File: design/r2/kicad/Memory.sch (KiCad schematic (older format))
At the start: 8 parts, among them U1 SST39SF040, U2 SST39SF040, U3 AS6C4008-55PCN, U4 AS6C4008-55PCN

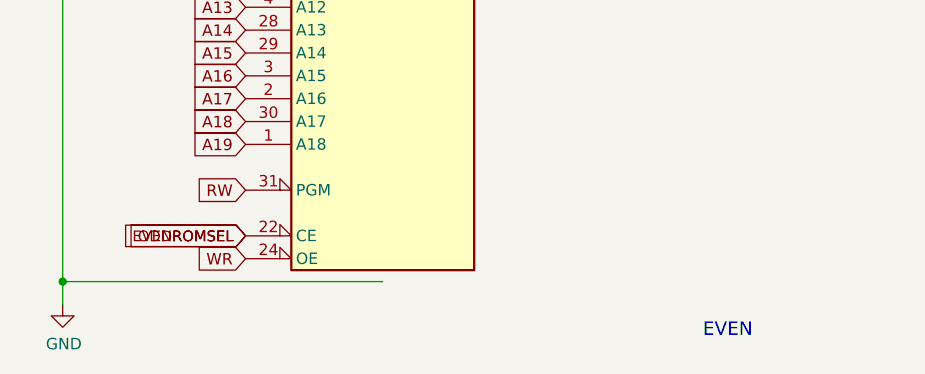
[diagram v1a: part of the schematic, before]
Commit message: Schematic / GAL tweaks and do layout
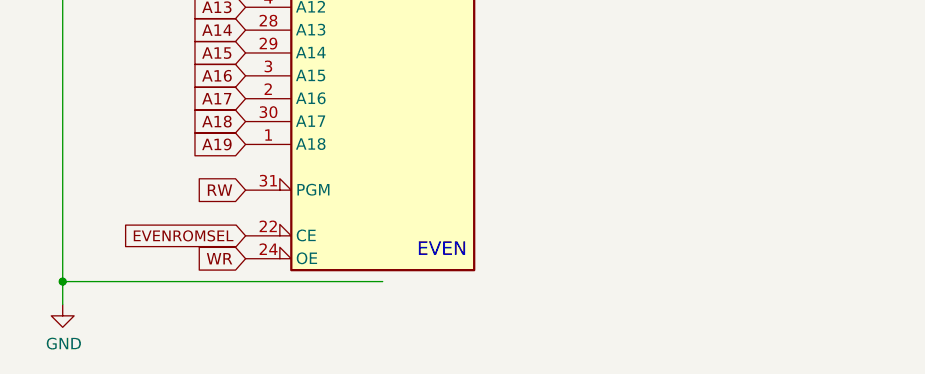
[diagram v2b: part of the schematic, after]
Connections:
- net EVENROMSEL: no longer U1.22 (CE)
- new net ODDROMSEL: U1.22 (CE)
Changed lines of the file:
@@
 Text Notes 6200 3900 0    59   ~ 0
 ODD
-Text Notes 3800 7600 0    59   ~ 0
+Text Notes 2550 7250 0    59   ~ 0
 EVEN
 Text Notes 9600 3900 0    59   ~ 0
@@
 Text GLabel 1800 7250 0    50   Input ~ 0
 WR
-Text GLabel 1800 7150 0    47   Input ~ 0
-ODDROMSEL
 $Comp
 L power:VCC #PWR0105

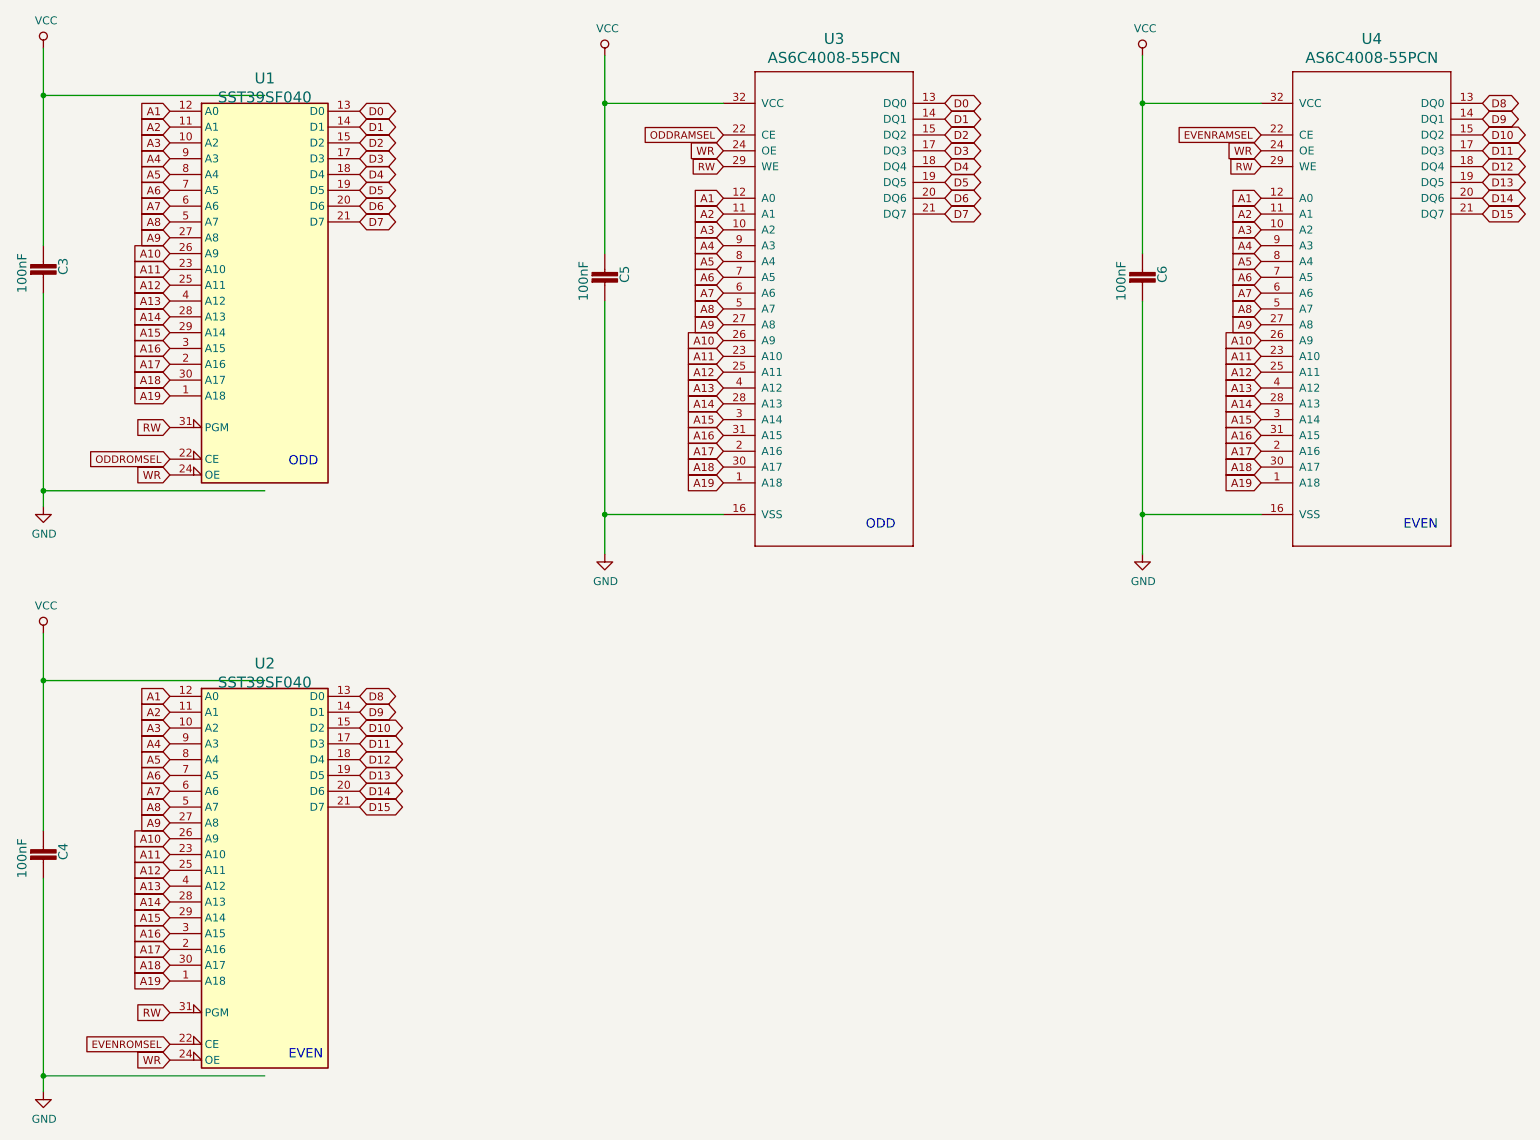
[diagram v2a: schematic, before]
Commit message: Add ROM write-enable jumper and tidy up
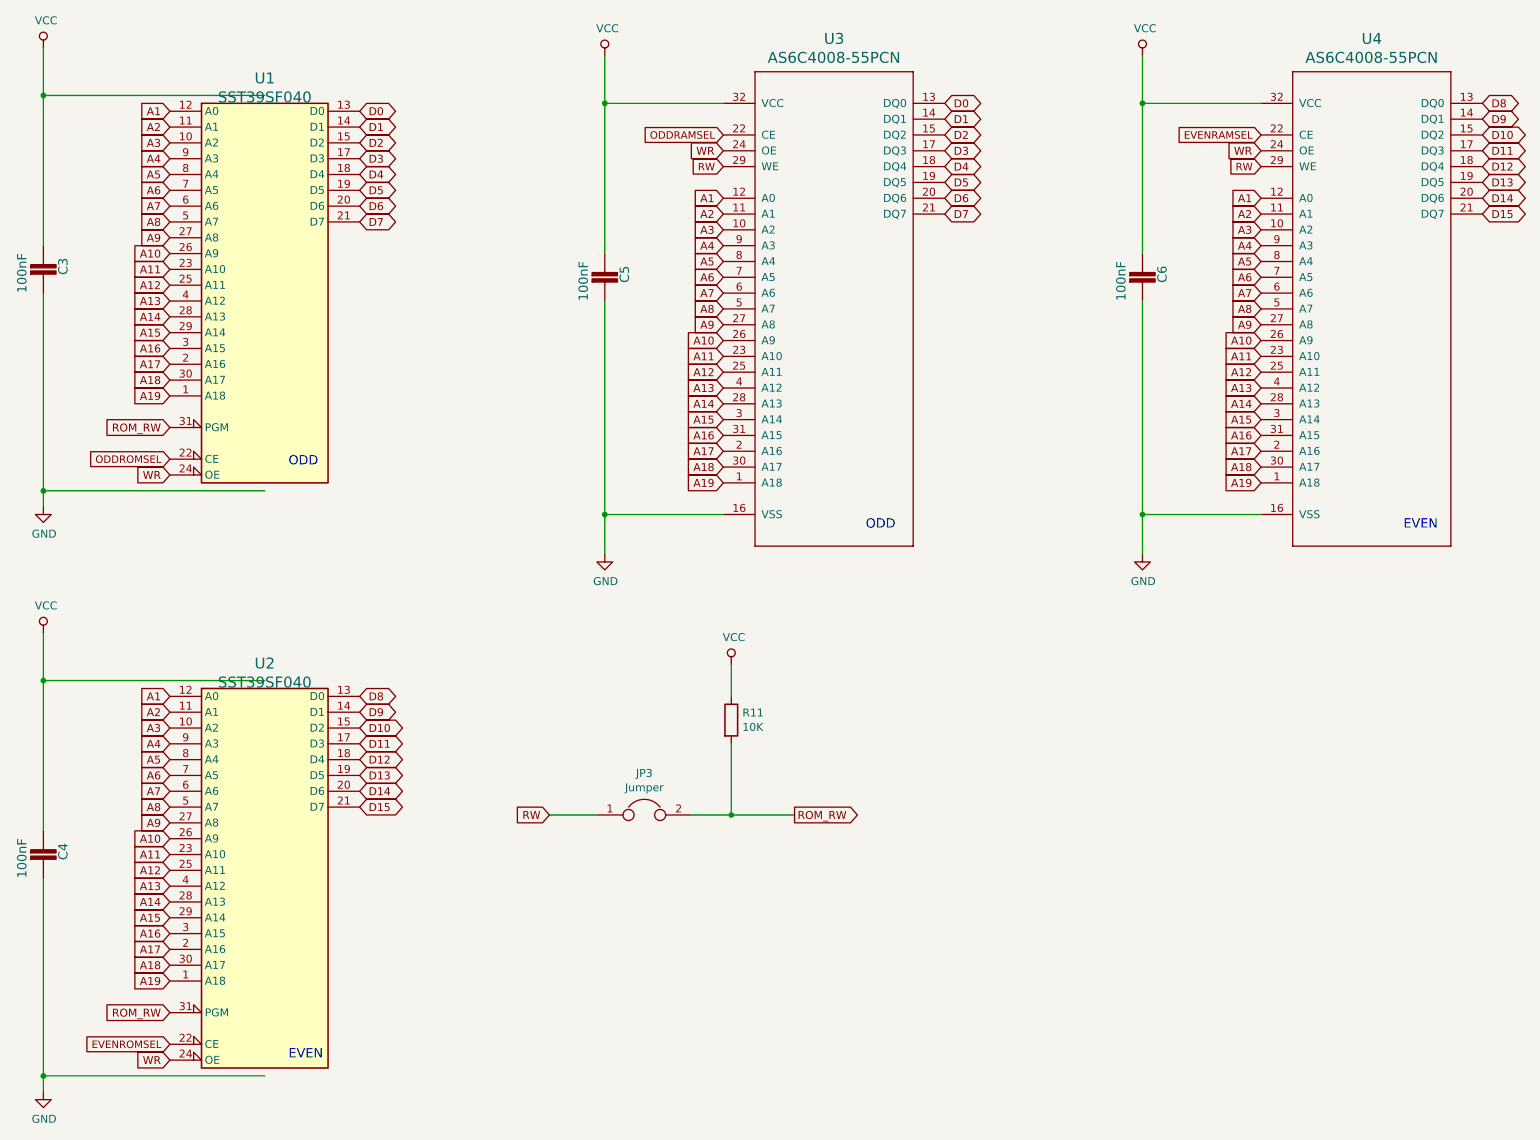
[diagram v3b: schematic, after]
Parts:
- added JP3: Jumper, rosco_m68k:1X02, symbol Device:Jumper
- added R11: 10K, rosco_m68k:0207_10, symbol Device:R
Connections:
- net RW: now also JP3.1; no longer U1.31 (PGM), U2.31 (PGM)
- net VCC: now also R11.1
- new net ROM_RW: JP3.2, R11.2, U1.31 (PGM), U2.31 (PGM)
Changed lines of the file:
@@
 D7
 Text GLabel 1800 3250 0    50   Input ~ 0
-RW
+ROM_RW
 Text GLabel 1800 3550 0    50   Input ~ 0
 WR
@@
 A19
 Text GLabel 1800 6950 0    50   Input ~ 0
-RW
+ROM_RW
 Text GLabel 1800 7250 0    50   Input ~ 0
 WR
@@
 Text GLabel 5300 1500 0    50   Input ~ 0
 WR
+$Comp
+L Device:Jumper JP3
+U 1 1 6162CC16
+P 4800 5700
+F 0 "JP3" H 4800 5964 50  0000 C CNN
+F 1 "Jumper" H 4800 5873 50  0000 C CNN
+F 2 "rosco_m68k:1X02" H 4800 5700 50  0001 C CNN
+F 3 "~" H 4800 5700 50  0001 C CNN
+	1    4800 5700
+	1    0    0    -1
+$EndComp
+Text GLabel 4200 5700 0    50   Input ~ 0
+RW
+Text GLabel 5750 5700 2    50   Output ~ 0
+ROM_RW
+Wire Wire Line
+	4200 5700 4500 5700
+Wire Wire Line
+	5100 5700 5350 5700
+$Comp
+L Device:R R11
+U 1 1 6162E070
+P 5350 5100
+F 0 "R11" H 5420 5146 50  0000 L CNN
+F 1 "10K" H 5420 5055 50  0000 L CNN
+F 2 "rosco_m68k:0207_10" V 5280 5100 50  0001 C CNN
+F 3 "~" H 5350 5100 50  0001 C CNN
+	1    5350 5100
+	1    0    0    -1
+$EndComp
+$Comp
+L power:VCC #PWR0114
+U 1 1 6162EC39
+P 5350 4750
+F 0 "#PWR0114" H 5350 4600 50  0001 C CNN
+F 1 "VCC" H 5367 4923 50  0000 C CNN
+F 2 "" H 5350 4750 50  0001 C CNN
+F 3 "" H 5350 4750 50  0001 C CNN
+	1    5350 4750
+	1    0    0    -1
+$EndComp
+Wire Wire Line
+	5350 4750 5350 4950
+Wire Wire Line
+	5350 5250 5350 5700
+Connection ~ 5350 5700
+Wire Wire Line
+	5350 5700 5750 5700
 $EndSCHEMATC
